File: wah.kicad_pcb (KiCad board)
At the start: 4 copper layers, 99.1 x 54.5 mm, 38 parts, among them J1 Barrel_Jack_Switch, J2 In, J3 Out, SW1 SW_Push_3PDT, U1 TL072, U2 L78L05_TO92

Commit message: fix errors
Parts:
- removed C10: 100u, Capacitor_THT:C_Rect_L7.0mm_W2.5mm_P5.00mm
- added C13: 100u, Capacitor_THT:CP_Radial_D6.3mm_P2.50mm, F.Cu at (47.7, 75.0)
- added TP_5V1: TestPoint, TestPoint:TestPoint_THTPad_1.5x1.5mm_Drill0.7mm, F.Cu at (128.7, 78.4)
- added TP_VREF1: TestPoint, TestPoint:TestPoint_THTPad_1.5x1.5mm_Drill0.7mm, F.Cu at (128.7, 83.6)
- C3: footprint Capacitor_THT:C_Rect_L7.0mm_W2.5mm_P5.00mm -> Capacitor_THT:CP_Radial_D6.3mm_P2.50mm
- moved G*** 105.3 mm to (75.5, 38.8)
- moved J2 55.6 mm to (105.3, 53.2), turned to 90 degrees
- moved D1 51.7 mm to (61.9, 48.3), turned to -90 degrees
- moved U2 41.9 mm to (59.6, 61.8)
- moved R5 40.1 mm to (63.9, 44.0)
- moved C4 37.1 mm to (63.9, 70.6), turned to 180 degrees
- moved C5 36.3 mm to (63.9, 75.1), turned to 180 degrees
- moved R6 34.8 mm to (59.8, 36.4)
- moved G*** 34.4 mm to (46.2, 65.3)
- moved J1 34.4 mm to (56.6, 65.3)
- moved SW1 33.9 mm to (132.2, 60.6)
- moved C6 33.9 mm to (88.7, 56.4)
- moved R4 33.9 mm to (87.4, 47.1)
- moved R8 33.9 mm to (99.9, 61.9)
- moved R9 33.9 mm to (126.3, 48.4)
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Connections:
- C11 pad 1: /FX_IN -> /AUDIO_OUT
- C6 pad 2: /FX_OUT -> /AUDIO_IN
- C9 pad 1: /FX_IN -> /AUDIO_OUT
- R1 pad 1: /AUDIO_OUT -> /FX_IN
- R4 pad 1: /FX_OUT -> /AUDIO_IN
- U1 pad 1: /AUDIO_IN -> /FX_OUT
- U1 pad 2: /AUDIO_IN -> /FX_OUT
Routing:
- net Net-(U1C-V+): track 83.0 -> 128.3 mm
- net /AUDIO_OUT: track 5.13 -> 48.0 mm
- net /FX_IN: track 60.7 -> 90.5 mm
- net Net-(J2-PadT): track 13.3 -> 39.8 mm
- net Net-(J3-PadT): track 30.4 -> 14.1 mm
- net /AUDIO_IN: track 28.7 -> 16.8 mm
- net Net-(D1-A): track 11.0 -> 15.2 mm
- net /FX_OUT: track 66.0 -> 63.7 mm
- net /POT1: track 16.5 -> 17.7 mm
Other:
- board text added: "Wah version 0.3"
- board text removed: "Wah version 0.2"

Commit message: reaarange power
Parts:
- moved D1 16.8 mm to (45.1, 49.0)
- moved R5 14.7 mm to (49.2, 44.7)
- moved R6 14.7 mm to (45.1, 37.1)
- moved RV1 9.00 mm to (64.9, 56.1)
- moved RV2 9.00 mm to (64.9, 42.7)
- moved U2 2.14 mm to (61.7, 61.4), turned to -90 degrees
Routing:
- net /POT2: track 12.1 -> 3.06 mm
- net /POT1: track 17.7 -> 13.4 mm
- net Net-(D1-A): track 15.2 -> 10.9 mm
- net Net-(U1C-V+): track 128.3 -> 131.5 mm
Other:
- board text added: "Vintage 1952 NOS ElectroSmith Daisy"
- board text added: "Wah version 0.4"
- board text removed: "Vintage 1951 NOS ElectroSmith Daisy"
- board text removed: "Wah version 0.3"
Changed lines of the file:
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@@
 	(title_block
 		(title "Wah")
-		(date "2025-10-31")
-		(rev "0.3")
+		(date "2025-11-01")
+		(rev "0.4")
 		(company "KnightHill Engineering")
 	)
@@
 	(footprint "Diode_THT:D_A-405_P7.62mm_Horizontal"
 		(layer "F.Cu")
-		(at 61.885 48.27 -90)
+		(at 45.1 49.035 -90)
 		(descr "Diode, A-405 series, Axial, Horizontal, pin pitch=7.62mm, , length*diameter=5.2*2.7mm^2, , http://www.diodes.com/_files/packages/A-405.pdf")
 		(tags "Diode A-405 series Axial Horizontal pin pitch 7.62mm  length 5.2mm diameter 2.7mm")
@@
 	(footprint "CustomFootprints:Potentiometer_uxcel_9mm_Single_Vertical"
 		(layer "F.Cu")
-		(at 55.947 42.7316 180)
+		(at 64.947 42.7316 180)
 		(descr "Potentiometer, vertical, 9mm, single, http://www.taiwanalpha.com.tw/downloads?target=products&id=113")
 		(tags "potentiometer vertical 9mm single")
@@
 	(footprint "Resistor_THT:R_Axial_DIN0207_L6.3mm_D2.5mm_P7.62mm_Horizontal"
 		(layer "F.Cu")
-		(at 59.785 36.36 -90)
+		(at 45.1 37.125 -90)
 		(descr "Resistor, Axial_DIN0207 series, Axial, Horizontal, pin pitch=7.62mm, 0.25W = 1/4W, length*diameter=6.3*2.5mm^2, http://cdn-reichelt.de/documents/datenblatt/B400/1_4W%23YAG.pdf")
 		(tags "Resistor Axial_DIN0207 series Axial Horizontal pin pitch 7.62mm 0.25W = 1/4W length 6.3mm diameter 2.5mm")
@@
 	(footprint "Package_TO_SOT_THT:TO-92_Inline_Wide"
 		(layer "F.Cu")
-		(at 59.645 61.83)
+		(at 61.74 61.395 -90)
 		(descr "TO-92 leads in-line, wide, drill 0.75mm (see NXP sot054_po.pdf)")
 		(tags "to-92 sc-43 sc-43a sot54 PA33 transistor")
 		(property "Reference" "U2"
-			(at 5.24 -2.76 0)
+			(at 5.24 -2.76 90)
 			(layer "F.SilkS")
 			(effects
@@
 		)
 		(property "Value" "L78L05_TO92"
-			(at 2.54 2.79 0)
+			(at 2.54 2.79 90)
 			(layer "F.Fab")
 			(effects
@@
 		)
 		(property "Datasheet" "http://www.st.com/content/ccc/resource/technical/document/datasheet/15/55/e5/aa/23/5b/43/fd/CD00000446.pdf/files/CD00000446.pdf/jcr:content/translations/en.CD00000446.pdf"
-			(at 0 0 0)
+			(at 0 0 270)
 			(unlocked yes)
 			(layer "F.Fab")
@@
 		)
 		(property "Description" "Positive 100mA 30V Linear Regulator, Fixed Output 5V, TO-92"
-			(at 0 0 0)
+			(at 0 0 270)
 			(unlocked yes)
 			(layer "F.Fab")
@@
 		)
 		(fp_arc
-			(start 0.1836 -1.098807)
-			(mid 1.143021 -2.192817)
-			(end 2.54 -2.6)
+			(start 0.74 1.85)
+			(mid 0.446097 1.509328)
+			(end 0.215816 1.122795)
 			(stroke
 				(width 0.12)
@@
 		)
 		(fp_arc
-			(start 0.74 1.85)
-			(mid 0.446097 1.509328)
-			(end 0.215816 1.122795)
+			(start 4.864184 1.122795)
+			(mid 4.633903 1.509328)
+			(end 4.34 1.85)
 			(stroke
 				(width 0.12)
@@
 		)
 		(fp_arc
-			(start 2.54 -2.6)
-			(mid 3.936979 -2.192818)
-			(end 4.8964 -1.098807)
+			(start 0.1836 -1.098807)
+			(mid 1.143021 -2.192817)
+			(end 2.54 -2.6)
 			(stroke
 				(width 0.12)
@@
 		)
 		(fp_arc
-			(start 4.864184 1.122795)
-			(mid 4.633903 1.509328)
-			(end 4.34 1.85)
+			(start 2.54 -2.6)
+			(mid 3.936979 -2.192818)
+			(end 4.8964 -1.098807)
 			(stroke
 				(width 0.12)
@@
 		)
 		(fp_line
-			(start -1.01 -2.73)
+			(start 6.09 2.01)
 			(end -1.01 2.01)
 			(stroke
@@
 		)
 		(fp_line
-			(start -1.01 -2.73)
+			(start 6.09 2.01)
 			(end 6.09 -2.73)
 			(stroke
@@
 		)
 		(fp_line
-			(start 6.09 2.01)
+			(start -1.01 -2.73)
 			(end -1.01 2.01)
 			(stroke
@@
 		)
 		(fp_line
-			(start 6.09 2.01)
+			(start -1.01 -2.73)
 			(end 6.09 -2.73)
 			(stroke
@@
 		)
 		(fp_text user "${REFERENCE}"
-			(at 2.54 0 0)
+			(at 2.54 0 90)
 			(layer "F.Fab")
 			(effects
@@
 		)
 		(pad "1" thru_hole rect
-			(at 0 0)
+			(at 0 0 270)
 			(size 1.5 1.5)
 			(drill 0.8)
@@
 		)
 		(pad "2" thru_hole circle
-			(at 2.54 0)
+			(at 2.54 0 270)
 			(size 1.5 1.5)
 			(drill 0.8)
@@
 		)
 		(pad "3" thru_hole circle
-			(at 5.08 0)
+			(at 5.08 0 270)
 			(size 1.5 1.5)
 			(drill 0.8)
@@
 		)
 		(embedded_fonts no)
+		(model "${KICAD9_3DMODEL_DIR}/Connector_BarrelJack.3dshapes/BarrelJack_GCT_DCJ200-10-A_Horizontal.step"
+			(offset
+				(xyz 0 0 0)
+			)
+			(scale
+				(xyz 1 1 1)
+			)
+			(rotate
+				(xyz -0 -0 90)
+			)
+		)
 	)
 	(footprint "LOGO"
@@
 	(footprint "CustomFootprints:Potentiometer_uxcel_9mm_Single_Vertical"
 		(layer "F.Cu")
-		(at 55.947 56.052 180)
+		(at 64.947 56.052 180)
 		(descr "Potentiometer, vertical, 9mm, single, http://www.taiwanalpha.com.tw/downloads?target=products&id=113")
 		(tags "potentiometer vertical 9mm single")
@@
 	(footprint "Resistor_THT:R_Axial_DIN0207_L6.3mm_D2.5mm_P7.62mm_Horizontal"
 		(layer "F.Cu")
-		(at 63.885 43.98 90)
+		(at 49.2 44.745 90)
 		(descr "Resistor, Axial_DIN0207 series, Axial, Horizontal, pin pitch=7.62mm, 0.25W = 1/4W, length*diameter=6.3*2.5mm^2, http://cdn-reichelt.de/documents/datenblatt/B400/1_4W%23YAG.pdf")
 		(tags "Resistor Axial_DIN0207 series Axial Horizontal pin pitch 7.62mm 0.25W = 1/4W length 6.3mm diameter 2.5mm")
@@
 		(layer "Edge.Cuts")
 	)
-	(gr_text "Wah\nversion 0.3"
+	(gr_text "Wah\nversion 0.4"
 		(at 75.632 42.845059 0)
 		(layer "F.SilkS")
@@
 		)
 	)
-	(gr_text "Vintage 1951 NOS ElectroSmith Daisy"
+	(gr_text "Vintage 1952 NOS ElectroSmith Daisy"
 		(at 76.23375 75.436364 90)
 		(layer "F.SilkS")
@@
 	)
 	(segment
-		(start 55.947 53.552)
-		(end 59.305 53.552)
-		(width 0.5)
-		(layer "In1.Cu")
-		(net 13)
-	)
-	(segment
-		(start 66.711 44.0726)
-		(end 68.012 42.7716)
-		(width 0.5)
+		(start 64.947 53.552)
+		(end 63.346 51.951)
+		(width 1)
 		(layer "In1.Cu")
 		(net 13)
 	)
 	(segment
-		(start 66.711 46.146)
-		(end 66.711 44.0726)
-		(width 0.5)
+		(start 63.346 51.951)
+		(end 63.346 47.4376)
+		(width 1)
 		(layer "In1.Cu")
 		(net 13)
 	)
 	(segment
-		(start 59.305 53.552)
-		(end 66.711 46.146)
-		(width 0.5)
+		(start 63.346 47.4376)
+		(end 68.012 42.7716)
+		(width 1)
 		(layer "In1.Cu")
 		(net 13)
 	)
 	(segment
-		(start 55.947 40.2316)
+		(start 64.947 40.2316)
 		(end 68.012 40.2316)
-		(width 0.5)
+		(width 1)
 		(layer "In1.Cu")
 		(net 14)
@@
 	)
 	(segment
-		(start 63.885 57.59)
-		(end 59.645 61.83)
+		(start 65.6 65.255)
+		(end 61.74 61.395)
 		(width 1)
 		(layer "F.Cu")
@@
 	)
 	(segment
-		(start 61.5 77.168333)
-		(end 63.9 79.568333)
+		(start 61.74 57.285)
+		(end 61.74 61.395)
 		(width 1)
 		(layer "F.Cu")
@@
 	)
 	(segment
-		(start 63.885 43.98)
-		(end 63.885 57.59)
+		(start 49.2 44.745)
+		(end 61.74 57.285)
 		(width 1)
 		(layer "F.Cu")
@@
 	)
 	(segment
-		(start 59.645 61.83)
-		(end 61.5 63.685)
+		(start 65.6 77.868333)
+		(end 65.6 65.255)
 		(width 1)
 		(layer "F.Cu")
@@
 	)
 	(segment
-		(start 61.5 63.685)
-		(end 61.5 77.168333)
+		(start 63.9 79.568333)
+		(end 63.9 84.035)
 		(width 1)
 		(layer "F.Cu")
@@
 	(segment
 		(start 63.9 79.568333)
-		(end 63.9 84.035)
+		(end 65.6 77.868333)
 		(width 1)
 		(layer "F.Cu")
@@
 	)
 	(segment
-		(start 59.965 55.89)
-		(end 61.885 55.89)
+		(start 45.1 56.655)
+		(end 45.1 59.785)
 		(width 1)
 		(layer "F.Cu")
@@
 	)
 	(segment
-		(start 50.585 65.27)
-		(end 59.965 55.89)
+		(start 45.1 59.785)
+		(end 50.585 65.27)
 		(width 1)
 		(layer "F.Cu")

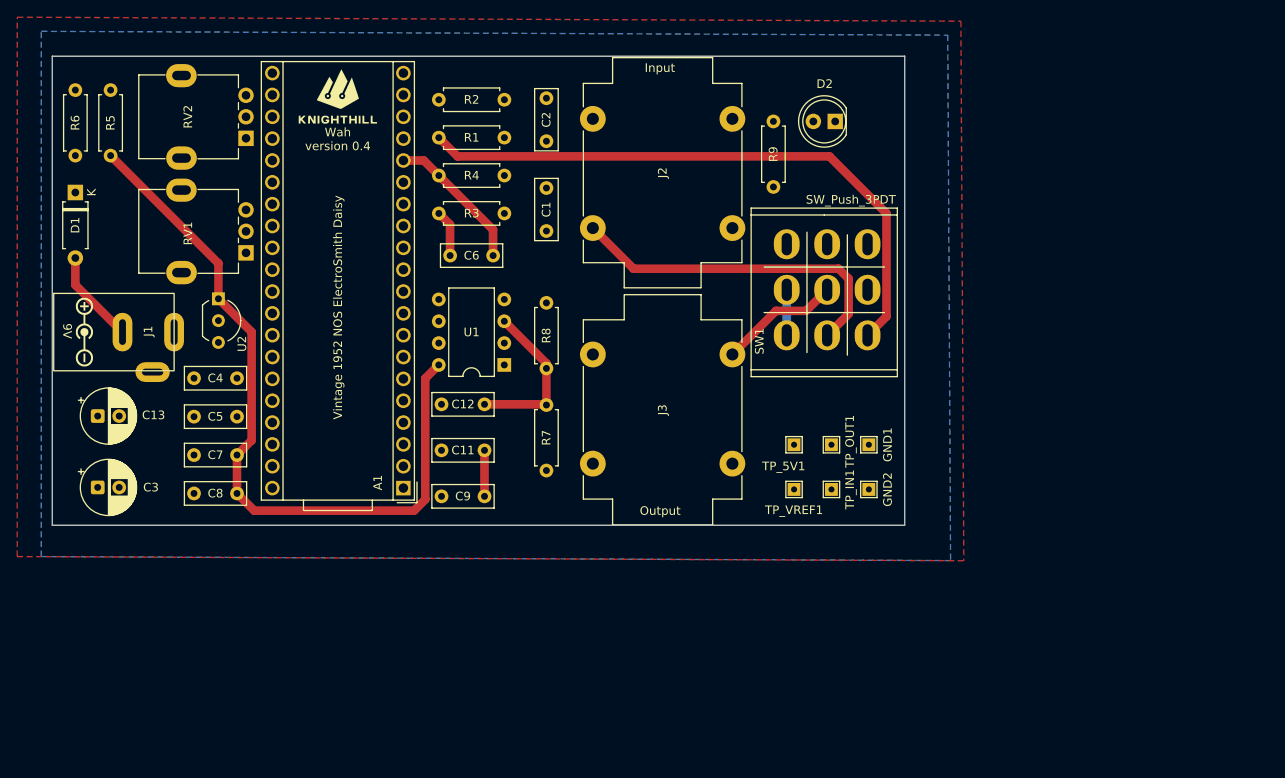
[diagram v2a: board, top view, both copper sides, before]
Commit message: add enclosure corners
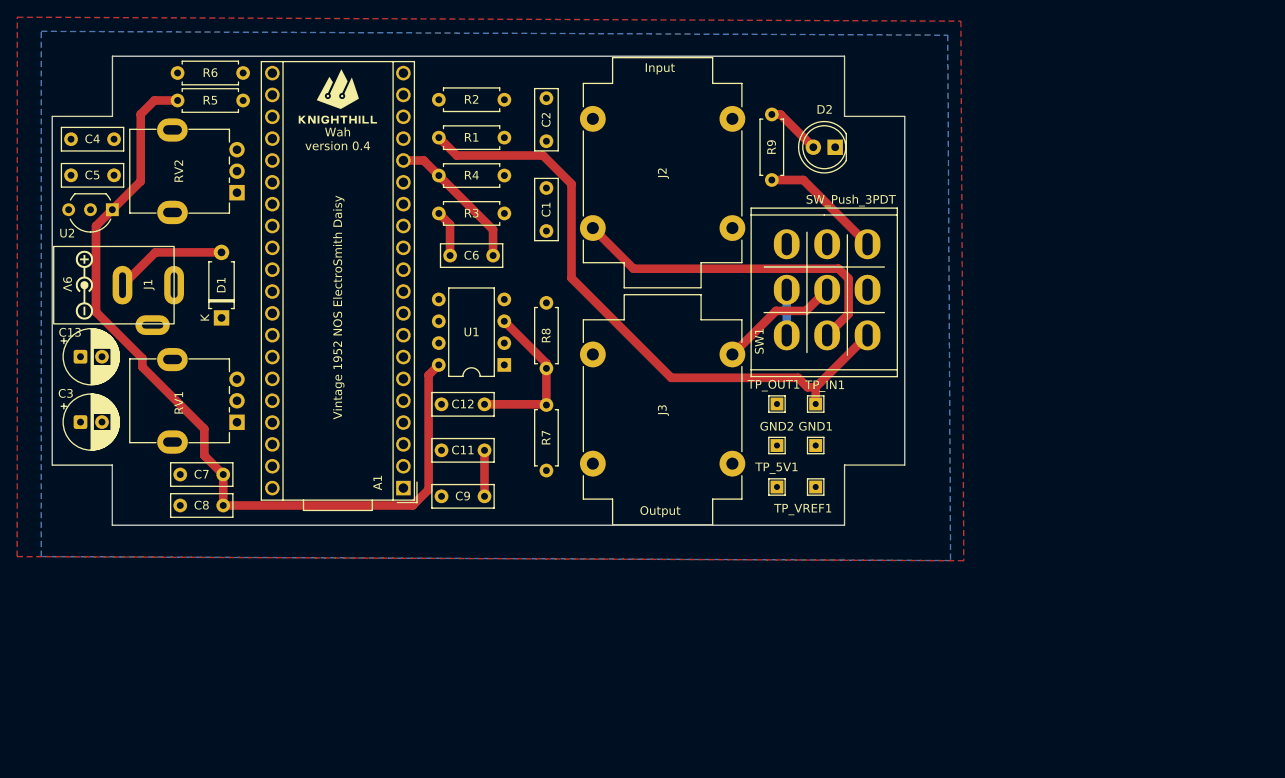
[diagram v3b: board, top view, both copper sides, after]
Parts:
- moved C5 34.1 mm to (44.6, 47.0), turned to 0 degrees
- moved C4 33.8 mm to (44.6, 42.8), turned to 0 degrees
- moved D1 22.4 mm to (62.1, 63.6), turned to 90 degrees
- moved RV1 19.7 mm to (63.9, 75.8)
- moved R6 19.6 mm to (64.6, 35.1), turned to 180 degrees
- moved U2 16.1 mm to (49.4, 51.0), turned to 180 degrees
- moved GND2 11.8 mm to (126.7, 78.5), turned to 90 degrees
- moved TP_IN1 10.1 mm to (131.2, 73.6)
- moved R5 10.1 mm to (57.0, 38.3), turned to 0 degrees
- moved TP_OUT1 7.91 mm to (126.7, 73.6)
- moved C3 7.86 mm to (45.7, 75.7)
- moved C13 7.18 mm to (45.7, 68.1)
- moved RV2 6.41 mm to (63.9, 49.1)
- moved GND1 6.19 mm to (131.2, 78.5), turned to 90 degrees
- moved G*** 5.46 mm to (46.2, 59.8)
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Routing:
- net /POT1: track 13.4 -> 32.2 mm
- net /FX_IN: track 90.5 -> 72.7 mm
- net Net-(U1C-V+): track 131.5 -> 143.6 mm
- net /POT2: track 3.06 -> 8.03 mm
- net /FX_OUT: track 63.7 -> 58.9 mm
- net Net-(D1-A): track 10.9 -> 13.1 mm
- net Net-(D2-A): track 4.65 -> 6.41 mm
- net Net-(R9-Pad1): track 13.7 -> 14.2 mm
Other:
- outline, holes or cut-outs redrawn

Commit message: improve pcb
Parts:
- moved R6 7.62 mm to (57.0, 35.1), turned to 0 degrees
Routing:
- net Net-(J2-PadT): track 39.8 -> 33.7 mm
- net /FX_IN: track 72.7 -> 73.5 mm
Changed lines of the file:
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@@
 		(tags "CP Radial series Radial pin pitch 2.50mm diameter 6.3mm height 7mm Electrolytic Capacitor")
 		(property "Reference" "C13"
-			(at -1.2 -2.8 0)
+			(at 6.5 -0.95 0)
 			(layer "F.SilkS")
 			(effects
@@
 	(footprint "Resistor_THT:R_Axial_DIN0207_L6.3mm_D2.5mm_P7.62mm_Horizontal"
 		(layer "F.Cu")
-		(at 64.61 35.135 180)
+		(at 56.99 35.135)
 		(descr "Resistor, Axial_DIN0207 series, Axial, Horizontal, pin pitch=7.62mm, 0.25W = 1/4W, length*diameter=6.3*2.5mm^2, http://cdn-reichelt.de/documents/datenblatt/B400/1_4W%23YAG.pdf")
 		(tags "Resistor Axial_DIN0207 series Axial Horizontal pin pitch 7.62mm 0.25W = 1/4W length 6.3mm diameter 2.5mm")
@@
 		(attr through_hole exclude_from_pos_files exclude_from_bom)
 		(fp_line
-			(start 7.08 1.37)
-			(end 7.08 1.04)
+			(start 0.54 -1.37)
+			(end 7.08 -1.37)
 			(stroke
 				(width 0.12)
@@
 		)
 		(fp_line
-			(start 7.08 -1.37)
-			(end 7.08 -1.04)
+			(start 0.54 -1.04)
+			(end 0.54 -1.37)
 			(stroke
 				(width 0.12)
@@
 		)
 		(fp_line
-			(start 0.54 1.37)
-			(end 7.08 1.37)
+			(start 0.54 1.04)
+			(end 0.54 1.37)
 			(stroke
 				(width 0.12)
@@
 		)
 		(fp_line
-			(start 0.54 1.04)
-			(end 0.54 1.37)
+			(start 0.54 1.37)
+			(end 7.08 1.37)
 			(stroke
 				(width 0.12)
@@
 		)
 		(fp_line
-			(start 0.54 -1.04)
-			(end 0.54 -1.37)
+			(start 7.08 -1.37)
+			(end 7.08 -1.04)
 			(stroke
 				(width 0.12)
@@
 		)
 		(fp_line
-			(start 0.54 -1.37)
-			(end 7.08 -1.37)
+			(start 7.08 1.37)
+			(end 7.08 1.04)
 			(stroke
 				(width 0.12)
@@
 		)
 		(fp_line
-			(start 7.62 0)
-			(end 6.96 0)
+			(start 0 0)
+			(end 0.66 0)
 			(stroke
 				(width 0.1)
@@
 		)
 		(fp_line
-			(start 0 0)
-			(end 0.66 0)
+			(start 7.62 0)
+			(end 6.96 0)
 			(stroke
 				(width 0.1)
@@
 		)
 		(pad "1" thru_hole circle
-			(at 0 0 180)
+			(at 0 0)
 			(size 1.6 1.6)
 			(drill 0.8)
@@
 		)
 		(pad "2" thru_hole circle
-			(at 7.62 0 180)
+			(at 7.62 0)
 			(size 1.6 1.6)
 			(drill 0.8)
@@
 	)
 	(segment
-		(start 129.15 70.585)
-		(end 130.25 71.685)
+		(start 137.235 68.32)
+		(end 137.235 65.65)
 		(width 1)
 		(layer "F.Cu")
@@
 	)
 	(segment
-		(start 89.455467 44.735)
-		(end 99.5 44.735)
+		(start 127.9 69.685)
+		(end 135.9 69.685)
+		(width 1)
+		(layer "F.Cu")
+		(net 28)
+	)
+	(segment
+		(start 137.25 68.335)
+		(end 137.235 68.32)
+		(width 1)
+		(layer "F.Cu")
+		(net 28)
+	)
+	(segment
+		(start 87.375 42.654533)
+		(end 89.455467 44.735)
 		(width 1)
 		(layer "F.Cu")
@@
 	(segment
 		(start 99.5 44.735)
-		(end 102.8 48.035)
+		(end 102.45 47.685)
 		(width 1)
 		(layer "F.Cu")
@@
 	)
 	(segment
-		(start 102.8 48.035)
-		(end 102.8 58.985)
+		(start 131.2 72.985)
+		(end 127.9 69.685)
 		(width 1)
 		(layer "F.Cu")
@@
 	)
 	(segment
-		(start 114.4 70.585)
-		(end 129.15 70.585)
+		(start 112.615 64.4)
+		(end 122.615 64.4)
 		(width 1)
 		(layer "F.Cu")
@@
 	)
 	(segment
-		(start 87.375 42.654533)
-		(end 89.455467 44.735)
+		(start 122.615 64.4)
+		(end 127.9 69.685)
 		(width 1)
 		(layer "F.Cu")
@@
 	)
 	(segment
-		(start 137.235 65.65)
-		(end 131.2 71.685)
+		(start 131.2 73.635)
+		(end 131.2 72.985)
 		(width 1)
 		(layer "F.Cu")
@@
 	)
 	(segment
-		(start 102.8 58.985)
-		(end 114.4 70.585)
+		(start 102.45 54.235)
+		(end 112.615 64.4)
 		(width 1)
 		(layer "F.Cu")
@@
 	)
 	(segment
-		(start 131.2 71.685)
-		(end 131.2 73.635)
+		(start 102.45 47.685)
+		(end 102.45 54.235)
+		(width 1)
+		(layer "F.Cu")
+		(net 28)
+	)
+	(segment
+		(start 89.455467 44.735)
+		(end 99.5 44.735)
 		(width 1)
 		(layer "F.Cu")
@@
 	)
 	(segment
-		(start 130.25 71.685)
-		(end 131.2 71.685)
+		(start 135.9 69.685)
+		(end 137.25 68.335)
 		(width 1)
 		(layer "F.Cu")
@@
 	)
 	(segment
-		(start 110.014 57.899)
-		(end 133.864 57.899)
-		(width 1)
-		(layer "F.Cu")
-		(net 50)
-	)
-	(segment
-		(start 135.034 63.151)
+		(start 130.084 63.199)
 		(end 132.535 65.65)
 		(width 1)
@@
 	)
 	(segment
-		(start 133.864 57.899)
-		(end 135.034 59.069)
+		(start 105.285 53.17)
+		(end 105.285 55.37153)
 		(width 1)
 		(layer "F.Cu")
@@
 	)
 	(segment
-		(start 135.034 59.069)
-		(end 135.034 63.151)
+		(start 105.285 55.37153)
+		(end 113.11247 63.199)
 		(width 1)
 		(layer "F.Cu")
@@
 	)
 	(segment
-		(start 105.285 53.17)
-		(end 110.014 57.899)
+		(start 113.11247 63.199)
+		(end 130.084 63.199)
 		(width 1)
 		(layer "F.Cu")
@@
 	)
 	(segment
-		(start 132.535 60.35)
-		(end 130.084 62.801)
+		(start 130.084 62.801)
+		(end 126.584 62.801)
 		(width 1)
-		(layer "F.Cu")
+		(layer "In2.Cu")
 		(net 52)
 	)
 	(segment
-		(start 130.084 62.801)
-		(end 126.584 62.801)
+		(start 132.535 60.35)
+		(end 130.084 62.801)
 		(width 1)
-		(layer "F.Cu")
+		(layer "In2.Cu")
 		(net 52)
 	)
@@
 		(end 121.515 67.87)
 		(width 1)
-		(layer "F.Cu")
+		(layer "In2.Cu")
 		(net 52)
 	)

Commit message: remove probes
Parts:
- removed TP_5V1, TP_VREF1: TestPoint, TestPoint:TestPoint_THTPad_1.5x1.5mm_Drill0.7mm
- moved C2 1.56 mm to (98.4, 42.7)
- moved C1 1.50 mm to (98.4, 48.5)
- moved R7 1.50 mm to (98.4, 81.4)
- moved R8 1.50 mm to (98.4, 61.9)
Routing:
- net Net-(U1C-V+): track 143.6 -> 98.4 mm
- net Net-(U1A-+): track 19.0 -> 16.9 mm
- net Net-(C11-Pad2): track 13.2 -> 11.7 mm
- net Net-(U1B-+): track 31.3 -> 30.0 mm
- net Net-(C1-Pad1): track 10.5 -> 9.25 mm

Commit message: polish pcb
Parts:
- moved R1 16.9 mm to (98.4, 55.5), turned to 90 degrees
- moved R2 15.6 mm to (95.0, 51.9), turned to 180 degrees
- moved C2 14.4 mm to (93.7, 56.3), turned to 180 degrees
- moved C6 14.2 mm to (93.7, 43.1), turned to 180 degrees
- moved R3 8.60 mm to (87.4, 47.5), turned to 0 degrees
- moved R4 8.42 mm to (87.4, 38.6)
- moved C9 8.32 mm to (88.7, 77.1), turned to 0 degrees
- moved C11 4.38 mm to (88.7, 80.8), turned to 0 degrees
- moved C1 4.27 mm to (98.4, 44.2), turned to 90 degrees
- moved C12 1.05 mm to (93.7, 73.4)
- moved R7 0.39 mm to (98.4, 81.0)
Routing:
- net /FX_IN: track 73.5 -> 53.3 mm
- net Net-(U1B-+): track 30.0 -> 10.7 mm
- net Net-(C11-Pad2): track 11.7 -> 4.78 mm
- net /AUDIO_IN: track 16.8 -> 11.3 mm
- net Net-(C1-Pad1): track 9.25 -> 14.0 mm
- net Net-(U1B--): track 18.2 -> 22.2 mm
- net Net-(J2-PadT): track 33.7 -> 36.9 mm
- net /AUDIO_OUT: track 48.0 -> 45.0 mm
- net Net-(U1A-+): track 16.9 -> 15.5 mm

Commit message: optimize pcb
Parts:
- moved R8 24.7 mm to (91.5, 85.6), turned to 0 degrees
- moved C1 11.6 mm to (92.8, 54.4), turned to 0 degrees
- moved R7 7.06 mm to (91.5, 82.4), turned to 0 degrees
- moved C2 6.95 mm to (97.8, 50.7)
- moved R2 6.40 mm to (99.1, 47.0)
- moved R3 5.88 mm to (91.5, 43.2)
- moved C6 5.40 mm to (97.8, 39.5)
- moved R4 4.97 mm to (91.5, 35.8)
- moved C11 4.41 mm to (92.8, 79.1)
- moved C9 4.25 mm to (92.8, 75.9)
- moved C12 4.14 mm to (97.8, 72.7)
- moved U1 4.09 mm to (99.1, 69.2)
- moved R1 2.67 mm to (99.1, 58.1), turned to 180 degrees
- moved D1 1.15 mm to (63.2, 63.6)
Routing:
- net Net-(U1C-V+): track 98.4 -> 107.9 mm
- net Net-(U1A-+): track 15.5 -> 23.9 mm
- net Net-(U1B-+): track 10.7 -> 17.9 mm
- net /AUDIO_IN: track 11.3 -> 16.2 mm
- net Net-(U1B--): track 22.2 -> 26.4 mm
- net /FX_OUT: track 58.9 -> 54.8 mm
- net Net-(C1-Pad1): track 14.0 -> 10.8 mm
- net Net-(C11-Pad2): track 4.78 -> 7.64 mm
- net /AUDIO_OUT: track 45.0 -> 42.9 mm
- net /FX_IN: track 53.3 -> 51.6 mm
- net Net-(D1-A): track 13.1 -> 14.2 mm
- net Net-(C6-Pad1): track 4.96 -> 4.26 mm
